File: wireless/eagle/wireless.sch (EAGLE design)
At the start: 52 parts, among them J1 S7036-ND, J2 S7036-ND, J3 1175-1864-ND, J4 503182-1852, J5 277-1578-ND, Q1 16 MHz, Q2 16MHz, T2 LD1086D2M33TR, U1 ATMEGA2560AU, U2 BME280, U3 ATMEGA328P-AUR, U4 TXB0108PWR, U5 LT1529CQ-5PBF, U6 TXB0108PWR, X1 B6B-EH-A(LF)(SN), X2 1751248, X5 1751248

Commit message: Pin fixes
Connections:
- new net FAN_PWM1: U1.(CLKO/ICP3/INT7)PE7
- net CURRENT_SENSOR: now also U1.PK5(ADC13/PCINT21); no longer U1.(A15)PC7
- net ENCODER_SENSE1: now also U1.PK7(ADC15/PCINT23)
- net ENCODER_SENSE2: now also U1.PK6(ADC14/PCINT22)
- net IRQ_5V: now also U1.PJ6(PCINT15); no longer U1.PH6(OC2B)
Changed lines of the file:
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@@
 <net name="CURRENT_SENSOR" class="0">
 <segment>
-<label x="139.7" y="134.62" size="1.27" layer="95" xref="yes"/>
-<pinref part="U1" gate="1" pin="(A15)PC7"/>
-<wire x1="129.54" y1="134.62" x2="139.7" y2="134.62" width="0.1524" layer="91"/>
+<label x="48.26" y="88.9" size="1.27" layer="95" rot="R180" xref="yes"/>
+<wire x1="58.42" y1="88.9" x2="48.26" y2="88.9" width="0.1524" layer="91"/>
+<pinref part="U1" gate="1" pin="PK5(ADC13/PCINT21)"/>
 </segment>
 </net>
@@
 <net name="IRQ_5V" class="0">
 <segment>
-<pinref part="U1" gate="1" pin="PH6(OC2B)"/>
-<wire x1="58.42" y1="45.72" x2="50.8" y2="45.72" width="0.1524" layer="91"/>
-<label x="50.8" y="45.72" size="1.27" layer="95" rot="MR0" xref="yes"/>
+<wire x1="58.42" y1="68.58" x2="50.8" y2="68.58" width="0.1524" layer="91"/>
+<label x="50.8" y="68.58" size="1.27" layer="95" rot="MR0" xref="yes"/>
+<pinref part="U1" gate="1" pin="PJ6(PCINT15)"/>
 </segment>
 </net>
@@
 </segment>
 </net>
+<net name="ENCODER_SENSE1" class="0">
+<segment>
+<label x="48.26" y="93.98" size="1.27" layer="95" rot="R180" xref="yes"/>
+<wire x1="58.42" y1="93.98" x2="48.26" y2="93.98" width="0.1524" layer="91"/>
+<pinref part="U1" gate="1" pin="PK7(ADC15/PCINT23)"/>
+</segment>
+</net>
+<net name="ENCODER_SENSE2" class="0">
+<segment>
+<label x="48.26" y="91.44" size="1.27" layer="95" rot="R180" xref="yes"/>
+<wire x1="58.42" y1="91.44" x2="48.26" y2="91.44" width="0.1524" layer="91"/>
+<pinref part="U1" gate="1" pin="PK6(ADC14/PCINT22)"/>
+</segment>
+</net>
+<net name="FAN_PWM1" class="0">
+<segment>
+<wire x1="134.62" y1="88.9" x2="129.54" y2="88.9" width="0.1524" layer="91"/>
+<pinref part="U1" gate="1" pin="(CLKO/ICP3/INT7)PE7"/>
+<label x="134.62" y="88.9" size="1.27" layer="95" xref="yes"/>
+</segment>
+</net>

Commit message: wireless fixes
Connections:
- removed net FAN_PWM1: U1.(CLKO/ICP3/INT7)PE7
- net FAN_PWM: now also U1.(CLKO/ICP3/INT7)PE7
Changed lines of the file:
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@@
 <?xml version="1.0" encoding="utf-8"?>
 <!DOCTYPE eagle SYSTEM "eagle.dtd">
-<eagle version="9.2.2">
+<eagle version="9.3.0">
 <drawing>
 <settings>
@@
 </segment>
 </net>
-<net name="FAN_PWM1" class="0">
+<net name="FAN_PWM" class="0">
 <segment>
 <wire x1="134.62" y1="88.9" x2="129.54" y2="88.9" width="0.1524" layer="91"/>
@@
 </sheet>
 </sheets>
-<errors>
-</errors>
 </schematic>
 </drawing>

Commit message: wireless review notes
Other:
- note added: "Label voltage"
- note added: "make switch same as from other chip"
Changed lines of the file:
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@@
 <wire x1="83.82" y1="88.9" x2="83.82" y2="134.62" width="0.1524" layer="97" style="shortdash"/>
 <text x="86.36" y="91.44" size="1.778" layer="97">Logic Board Connector</text>
+<text x="269.24" y="109.22" size="1.778" layer="97">Label voltage</text>
 </plain>
 <instances>
@@
 from NeoPixel Data Sheet</text>
 <text x="-40.64" y="116.84" size="1.778" layer="97">535-9041-ND &lt;- Crystal Part ID</text>
+<text x="83.82" y="132.08" size="1.778" layer="97">make switch same as from other chip</text>
 </plain>
 <instances>

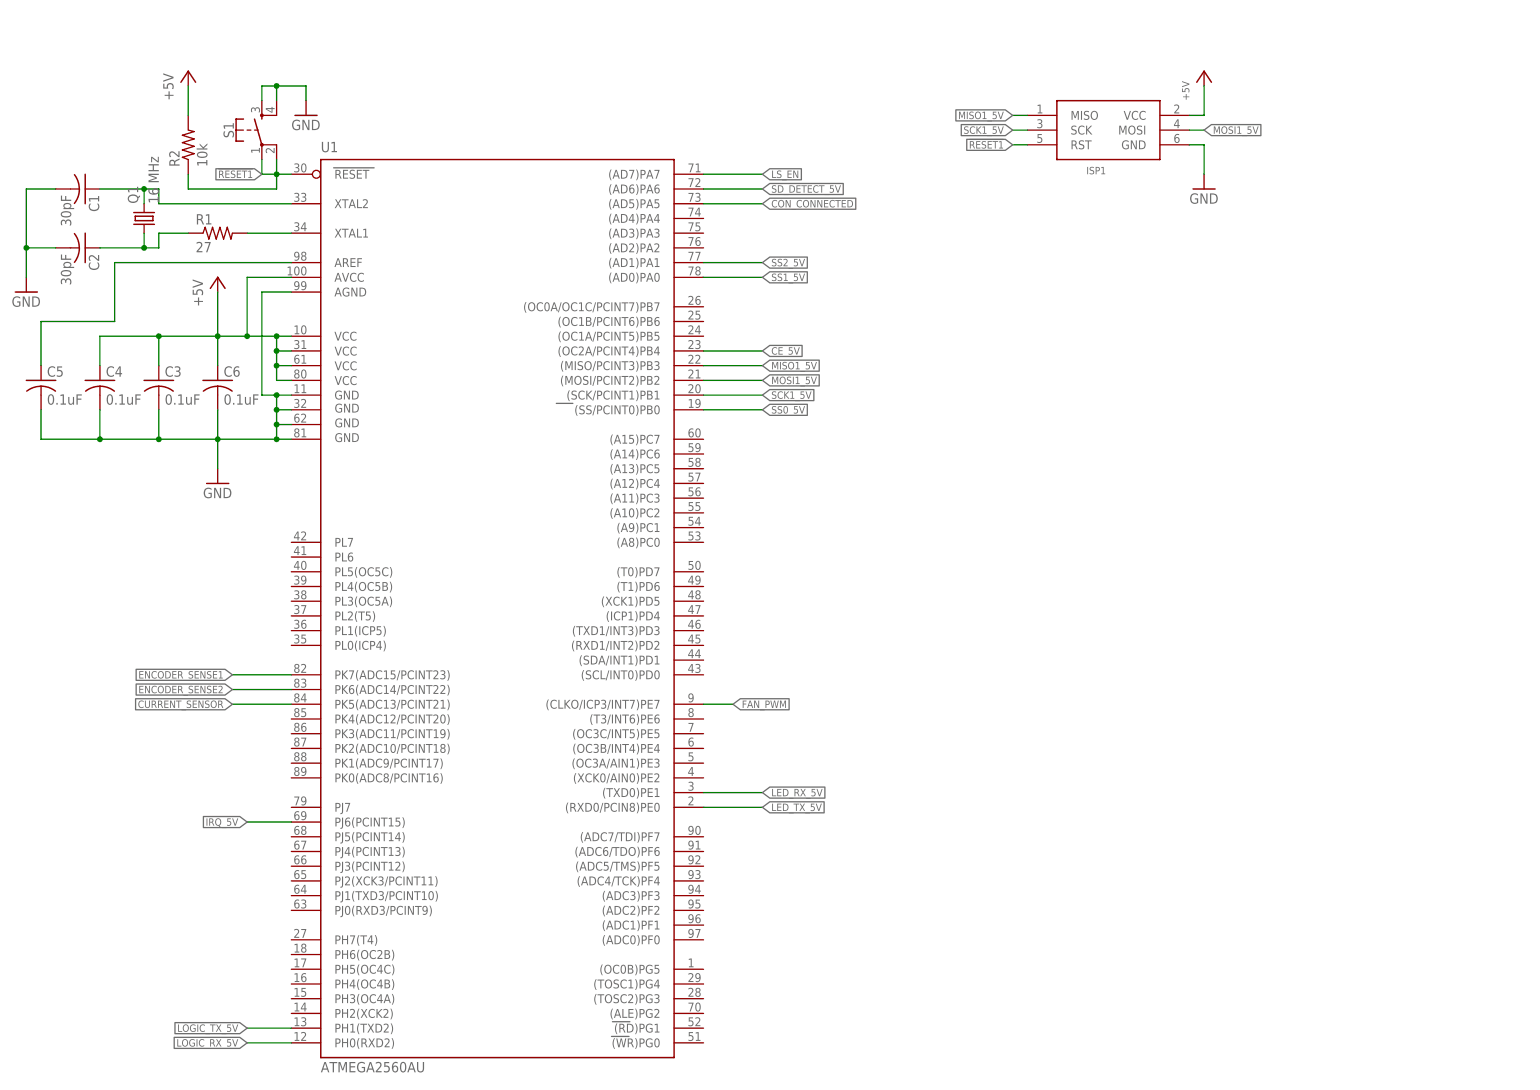
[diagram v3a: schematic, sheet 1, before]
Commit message: Fix capacitors
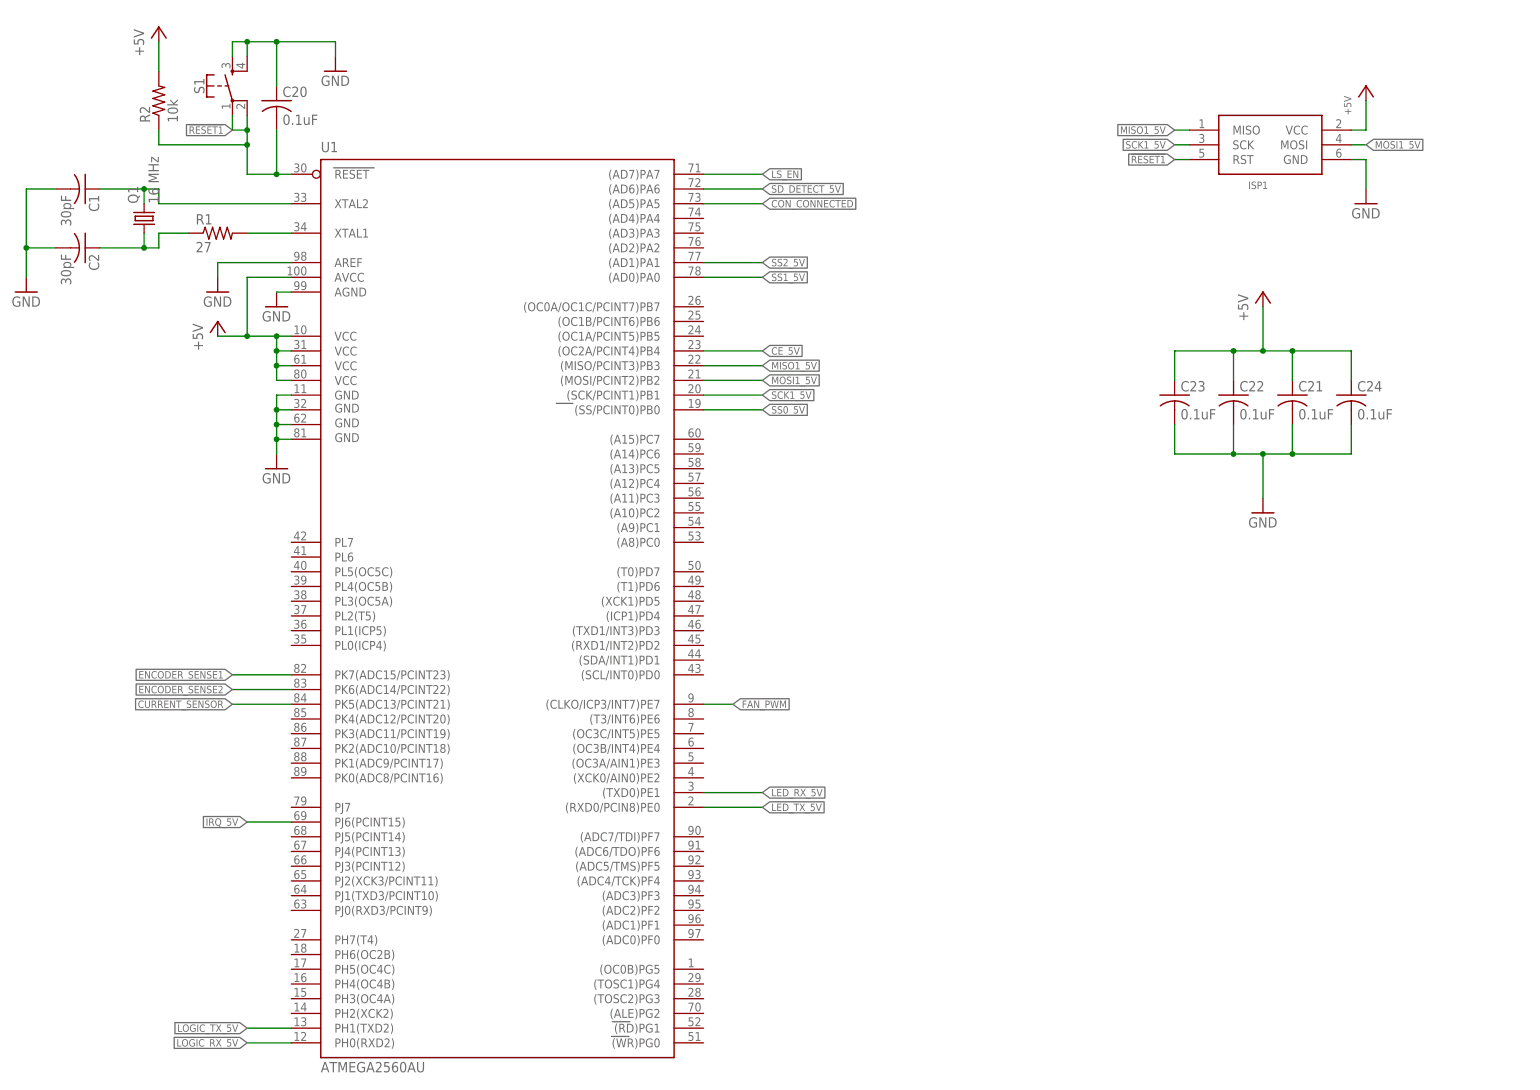
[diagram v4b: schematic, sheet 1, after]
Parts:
- removed C3, C4, C5, C6: 0.1uF, rcl:C-USC0603
- added C20, C21, C22, C23, C24: 0.1uF, rcl:C-USC0603
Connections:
- removed net N$4: C5.1, U1.AREF
- net !RESET1: now also C20.2
- net +5V: now also C21.1, C22.1, C23.1, C24.1; no longer C3.1, C4.1, C6.1
- net GND: now also C20.1, C21.2, C22.2, C23.2, C24.2, U1.AREF; no longer C3.2, C4.2, C5.2, C6.2
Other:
- moved on the sheet: ISP1, R2, S1

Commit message: fixes from design review
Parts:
- removed C10: 0.1 uF, SparkFun-Capacitors:1000UF-RADIAL-5MM-25V-20%
- removed S2: MOMENTARY-SWITCH-SPST-PTH-6.0MM-KIT, SparkFun-Switches:MOMENTARY-SWITCH-SPST-PTH-6.0MM-KIT
- removed U5: LT1529CQ-5PBF, LT1529CQ-5PBF:LT1529CQ-5PBF
- added C25, C3, C4, C5, C6: 0.1uF, rcl:C-USC0603
- added C26: 30pF, rcl:C-USC0603
- added C27: .1uF, rcl:C-USC0603
- added C28: 1000uf, rcl:C-USC0603
- added S3: (no value), SparkFun-Switches:MOMENTARY-SWITCH-SPST-2-SMD-5.2MM
- added U7: LM2678SX-5.0/NOPB, LM2678SX-5.0_NOPB:LM2678SX-5.0/NOPB
- C7, C8: value 22pF -> 30pF; device SparkFun-Capacitors:0.22UF-0603-25V-10% -> rcl:C-USC0603
- C9: value 1000uF -> .1uf; device SparkFun-Capacitors:1000UF-RADIAL-5MM-25V-20% -> rcl:C-USC0603
- R4: value 200 -> 1k
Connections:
- removed net GND1: U5.VIN, X5-2.K
- removed net N$22: D1.C, R4.1
- new net N$4: D1.A, R4.2
- net +5V: now also C25.1, C3.1, C4.1, C5.1, C6.1; no longer U5.OUTPUT, U5.SENSE/ADJ
- net +5V_FUSE: now also C28.1, R4.1; no longer C9.+, D1.A
- net GND: now also C25.2, C27.2, C28.2, C3.2, C4.2, C5.2, C6.2, C9.2, D1.C, S3.1, S3.2; no longer C10.-, C9.-, R4.2, S2.2, U5.GND, U5.GND_2, X5-1.K
- net N$23: now also C27.1; no longer C10.+
- net RST: now also C9.1, S3.3, S3.4; no longer S2.1
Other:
- note added: "8V"
- note removed: "Label voltage"
- note removed: "make switch same as from other chip"
- moved on the sheet: C17, C21, C22, C23, C24, D1, ISP1, J4, R10, R4, X5-1, X5-2

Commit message: Finished Design Review Changes
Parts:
- removed U7: LM2678SX-5.0/NOPB, LM2678SX-5.0_NOPB:LM2678SX-5.0/NOPB
- added C10: 22uF, rcl:C-USC0603
- added C29: .1uF, rcl:C-USC0603
- added C30, C31: 47uF, rcl:C-USC0603
- added R11: 56.2k, rcl:R-US_R0603
- added R12: 10k, rcl:R-US_R0603
- added U5: TPS565208DDCR, TPS565208DDCR:TPS565208DDCR
- added XAL6030-332MEB: 3.3uH, TPS565208DDCR:XAL6030-332MEB
- C17: device rcl:C-USC1206 -> rcl:C-USC0603
- C26: value 30pF -> .1uF
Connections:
- new net N$5: C10.1, C17.1, C26.1, U5.EN, U5.VIN, X5-1.K
- new net N$7: C29.2, U5.SW, XAL6030-332MEB.1
- new net N$8: C29.1, U5.VBST
- new net N$9: R11.1, R12.2, U5.VFB
- net +5V: now also C30.1, C31.1, R11.2, XAL6030-332MEB.2; no longer C17.1
- net GND: now also C10.2, C26.2, C30.2, C31.2, R12.1, U5.GND, X5-2.K
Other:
- note added: "+12V"
- note added: "GND"
- note added: "Voltage Regulator 12V to 5V (5A)"
- note removed: "8V"
- note removed: "Voltage Regulator 12V to 5V (3A)"
- moved on the sheet: C17, X5-1, X5-2

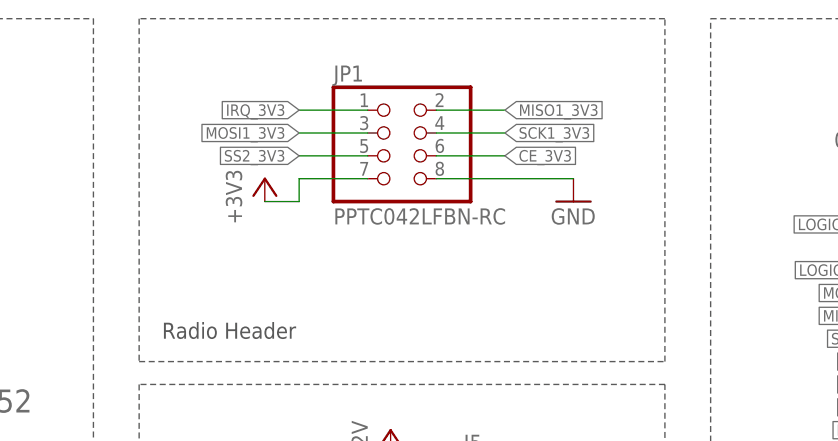
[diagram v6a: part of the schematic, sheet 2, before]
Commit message: Update Radio Header Connector
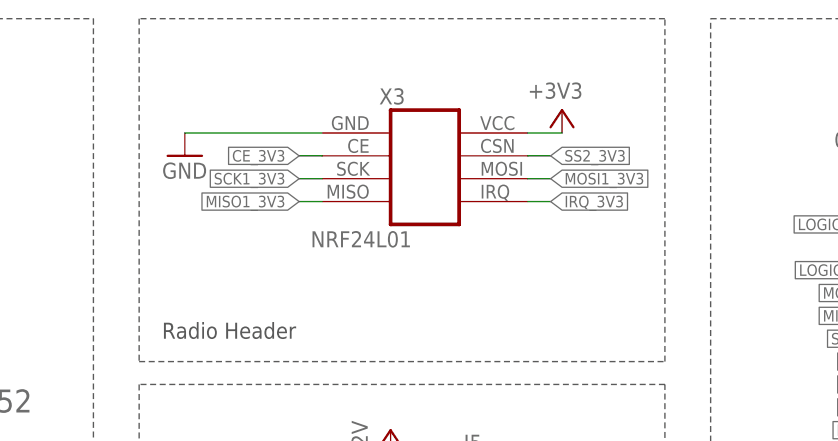
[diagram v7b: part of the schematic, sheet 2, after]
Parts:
- removed JP1: PPTC042LFBN-RC, pinhead:PINHD-2X4
- added X3: NRF24L01, IGVC-Connector:NRF24L01+PA+LNA
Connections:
- net +3.3V: now also X3.VCC; no longer JP1.7
- net CE_3V3: now also X3.CE; no longer JP1.6
- net GND: now also X3.GND; no longer JP1.8
- net IRQ_3V3: now also X3.IRQ; no longer JP1.1
- net MISO1_3V3: now also X3.MISO; no longer JP1.2
- net MOSI1_3V3: now also X3.MOSI; no longer JP1.3
- net SCK1_3V3: now also X3.SCK; no longer JP1.4
- net SS2_3V3: now also X3.CSN; no longer JP1.5
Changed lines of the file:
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@@
 <part name="P+10" library="supply1" library_urn="urn:adsk.eagle:library:371" deviceset="+5V" device="" value="+12V"/>
 <part name="GND23" library="supply1" library_urn="urn:adsk.eagle:library:371" deviceset="GND" device=""/>
-<part name="JP1" library="pinhead" library_urn="urn:adsk.eagle:library:325" deviceset="PINHD-2X4" device="" package3d_urn="urn:adsk.eagle:package:22461/2" value="PPTC042LFBN-RC"/>
 <part name="SUPPLY7" library="supply1" library_urn="urn:adsk.eagle:library:371" deviceset="+3V3" device=""/>
 <part name="R10" library="rcl" library_urn="urn:adsk.eagle:library:334" deviceset="R-US_" device="R0603" package3d_urn="urn:adsk.eagle:package:23555/2" value="10k"/>
@@
 <part name="C31" library="rcl" library_urn="urn:adsk.eagle:library:334" deviceset="C-US" device="C0603" package3d_urn="urn:adsk.eagle:package:23616/2" value="47uF"/>
 <part name="P+12" library="supply1" library_urn="urn:adsk.eagle:library:371" deviceset="+5V" device="" value="+5V"/>
+<part name="X3" library="IGVC-Connector" deviceset="NRF24L01+PA+LNA" device="" package3d_urn="urn:adsk.eagle:package:22461/2" value="NRF24L01"/>
 </parts>
 <sheets>
@@
 <attribute name="VALUE" x="111.76" y="144.78" size="1.778" layer="96"/>
 </instance>
-<instance part="JP1" gate="A" x="114.3" y="193.04" smashed="yes">
-<attribute name="NAME" x="107.95" y="201.295" size="1.778" layer="95"/>
-<attribute name="VALUE" x="107.95" y="185.42" size="1.778" layer="96"/>
-</instance>
-<instance part="SUPPLY7" gate="G$1" x="100.33" y="190.5" smashed="yes">
-<attribute name="VALUE" x="97.79" y="185.42" size="1.778" layer="96" rot="R90"/>
+<instance part="SUPPLY7" gate="G$1" x="133.35" y="198.12" smashed="yes">
+<attribute name="VALUE" x="129.54" y="199.39" size="1.778" layer="96"/>
 </instance>
 <instance part="R10" gate="G$1" x="40.64" y="172.72" smashed="yes" rot="R90">
@@
 <attribute name="VALUE" x="38.1" y="160.02" size="1.778" layer="96"/>
 </instance>
-<instance part="GND24" gate="1" x="134.62" y="187.96" smashed="yes">
-<attribute name="VALUE" x="132.08" y="185.42" size="1.778" layer="96"/>
+<instance part="GND24" gate="1" x="91.44" y="193.04" smashed="yes">
+<attribute name="VALUE" x="88.9" y="190.5" size="1.778" layer="96"/>
 </instance>
 <instance part="C15" gate="G$1" x="162.56" y="114.3" smashed="yes">
@@
 <instance part="P+12" gate="1" x="304.8" y="73.66" smashed="yes">
 <attribute name="VALUE" x="307.34" y="76.2" size="1.778" layer="96" rot="R180"/>
+</instance>
+<instance part="X3" gate="A" x="119.38" y="190.5" smashed="yes">
+<attribute name="NAME" x="113.03" y="198.755" size="1.778" layer="95"/>
+<attribute name="VALUE" x="105.41" y="182.88" size="1.778" layer="96"/>
 </instance>
 </instances>
@@
 </segment>
 <segment>
-<pinref part="JP1" gate="A" pin="8"/>
-<wire x1="119.38" y1="190.5" x2="134.62" y2="190.5" width="0.1524" layer="91"/>
+<wire x1="106.68" y1="195.58" x2="91.44" y2="195.58" width="0.1524" layer="91"/>
 <pinref part="GND24" gate="1" pin="GND"/>
+<pinref part="X3" gate="A" pin="GND"/>
 </segment>
 <segment>
@@
 </segment>
 <segment>
-<pinref part="JP1" gate="A" pin="4"/>
-<wire x1="119.38" y1="195.58" x2="127" y2="195.58" width="0.1524" layer="91"/>
-<label x="127" y="195.58" size="1.27" layer="95" xref="yes"/>
+<wire x1="106.68" y1="190.5" x2="104.14" y2="190.5" width="0.1524" layer="91"/>
+<label x="104.14" y="190.5" size="1.27" layer="95" rot="R180" xref="yes"/>
+<pinref part="X3" gate="A" pin="SCK"/>
 </segment>
 </net>
@@
 </segment>
 <segment>
-<pinref part="JP1" gate="A" pin="3"/>
-<wire x1="111.76" y1="195.58" x2="104.14" y2="195.58" width="0.1524" layer="91"/>
-<label x="104.14" y="195.58" size="1.27" layer="95" rot="R180" xref="yes"/>
+<wire x1="129.54" y1="190.5" x2="132.08" y2="190.5" width="0.1524" layer="91"/>
+<label x="132.08" y="190.5" size="1.27" layer="95" xref="yes"/>
+<pinref part="X3" gate="A" pin="MOSI"/>
 </segment>
 </net>
@@
 </segment>
 <segment>
-<pinref part="JP1" gate="A" pin="2"/>
-<wire x1="119.38" y1="198.12" x2="127" y2="198.12" width="0.1524" layer="91"/>
-<label x="127" y="198.12" size="1.27" layer="95" xref="yes"/>
+<wire x1="106.68" y1="187.96" x2="104.14" y2="187.96" width="0.1524" layer="91"/>
+<label x="104.14" y="187.96" size="1.27" layer="95" rot="R180" xref="yes"/>
+<pinref part="X3" gate="A" pin="MISO"/>
 </segment>
 </net>
@@
 <net name="+3.3V" class="0">
 <segment>
-<pinref part="JP1" gate="A" pin="7"/>
-<wire x1="111.76" y1="190.5" x2="104.14" y2="190.5" width="0.1524" layer="91"/>
+<wire x1="129.54" y1="195.58" x2="133.35" y2="195.58" width="0.1524" layer="91"/>
 <pinref part="SUPPLY7" gate="G$1" pin="+3V3"/>
-<wire x1="104.14" y1="190.5" x2="104.14" y2="187.96" width="0.1524" layer="91"/>
-<wire x1="104.14" y1="187.96" x2="100.33" y2="187.96" width="0.1524" layer="91"/>
+<pinref part="X3" gate="A" pin="VCC"/>
 </segment>
 </net>
 <net name="CE_3V3" class="0">
 <segment>
-<pinref part="JP1" gate="A" pin="6"/>
-<wire x1="119.38" y1="193.04" x2="127" y2="193.04" width="0.1524" layer="91"/>
-<label x="127" y="193.04" size="1.27" layer="95" font="vector" xref="yes"/>
+<wire x1="106.68" y1="193.04" x2="104.14" y2="193.04" width="0.1524" layer="91"/>
+<label x="104.14" y="193.04" size="1.27" layer="95" font="vector" rot="R180" xref="yes"/>
+<pinref part="X3" gate="A" pin="CE"/>
 </segment>
 <segment>
@@
 <net name="IRQ_3V3" class="0">
 <segment>
-<pinref part="JP1" gate="A" pin="1"/>
-<wire x1="111.76" y1="198.12" x2="104.14" y2="198.12" width="0.1524" layer="91"/>
-<label x="104.14" y="198.12" size="1.27" layer="95" font="vector" rot="MR0" xref="yes"/>
+<wire x1="129.54" y1="187.96" x2="132.08" y2="187.96" width="0.1524" layer="91"/>
+<label x="132.08" y="187.96" size="1.27" layer="95" font="vector" rot="MR180" xref="yes"/>
+<pinref part="X3" gate="A" pin="IRQ"/>
 </segment>
 <segment>
@@
 </segment>
 <segment>
-<pinref part="JP1" gate="A" pin="5"/>
-<wire x1="111.76" y1="193.04" x2="104.14" y2="193.04" width="0.1524" layer="91"/>
-<label x="104.14" y="193.04" size="1.27" layer="95" font="vector" rot="MR0" xref="yes"/>
-</segment>
-</net>
+<wire x1="129.54" y1="193.04" x2="132.08" y2="193.04" width="0.1524" layer="91"/>
+<label x="132.08" y="193.04" size="1.27" layer="95" font="vector" rot="MR180" xref="yes"/>
+<pinref part="X3" gate="A" pin="CSN"/>
+</segment>
+</net>
